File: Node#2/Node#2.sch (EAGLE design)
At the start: 135 parts, among them IC1 TSL25911FN, J1 68712414522, Q1 BC847ALT1SMD, Q2 SI1308EDL-T1-GE3, Q3 FDN304PZ, U2 RV8564C3, U3 BLUENRG-232, U4 TPS63001DRCT, Y3 ECS-160-12-36-AGN-TR, Y4 NX2012SA-32.768K-STD-MUB-1

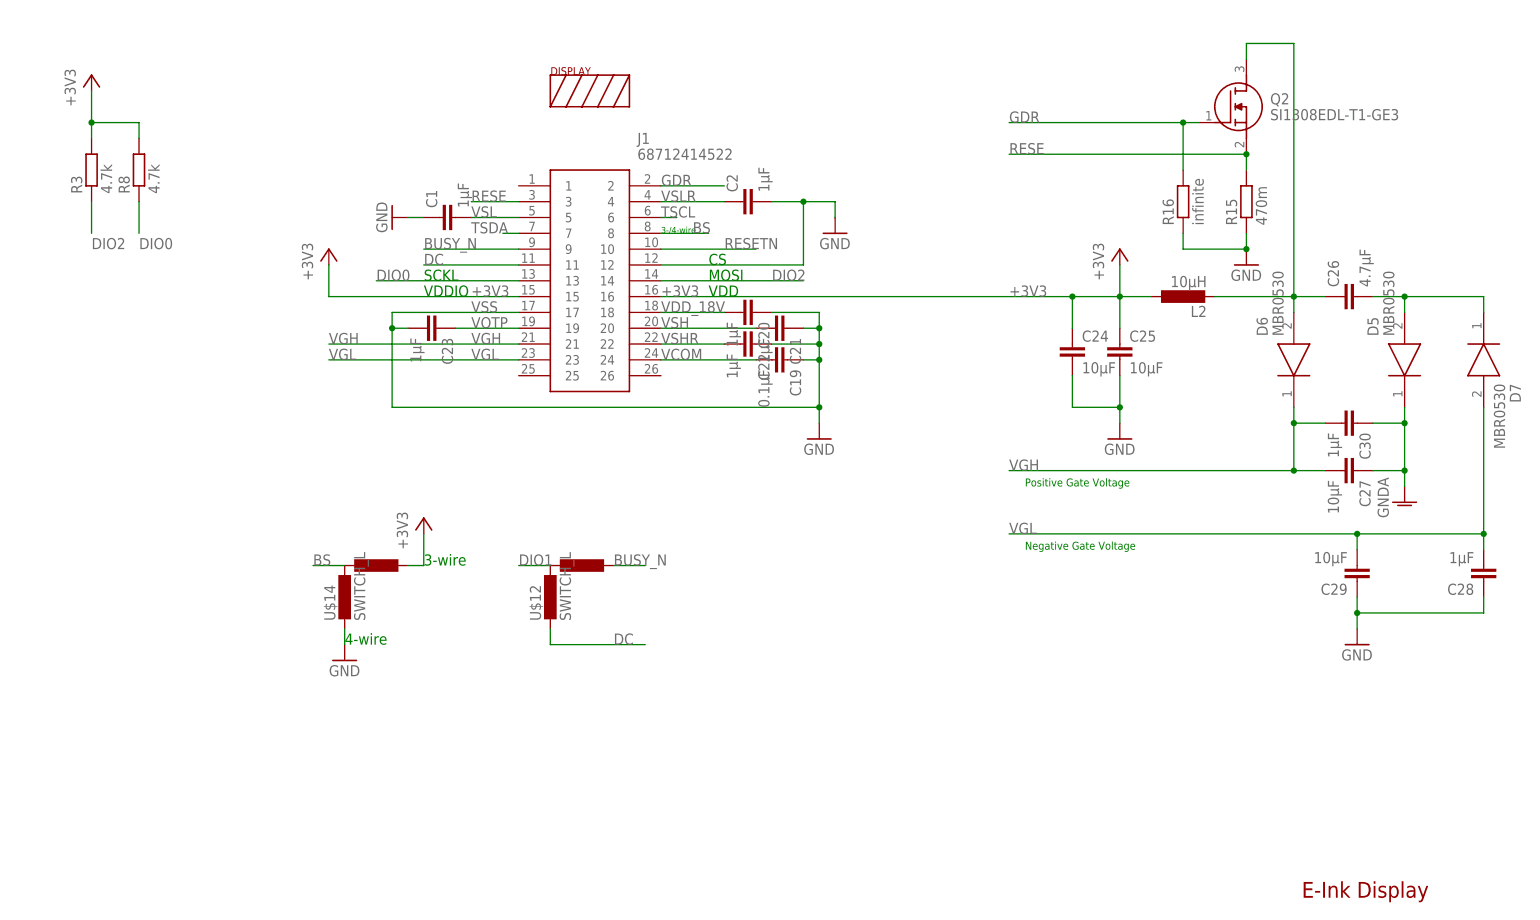
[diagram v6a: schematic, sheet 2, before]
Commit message: Finished Layout Node#2
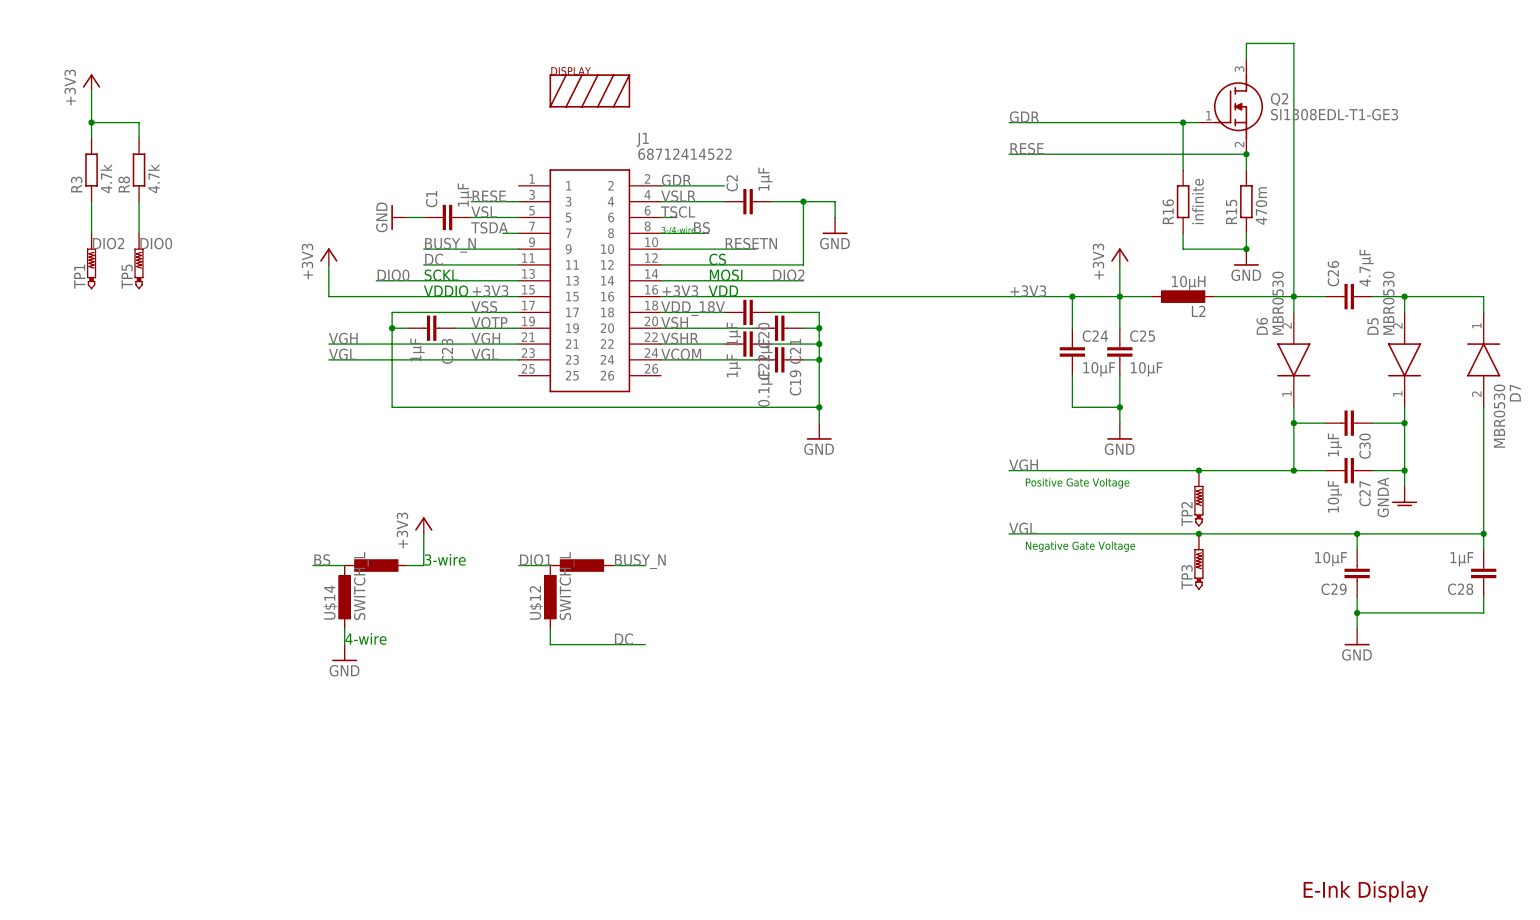
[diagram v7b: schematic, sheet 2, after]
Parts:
- removed D1: ZENER_SMB, BlueHome:ZENER_SMB
- removed U$7: PROXIMITY, BlueHome:PROXIMITY
- removed U$8: WHEEL, BlueHome:WHEEL
- added PROXI: PROXIMITY, BlueHome:PROXIMITY
- added TP1, TP2, TP3, TP4, TP5, TP6: PTR1TP20R, testpad:PTR1TP20R
- added U$18: BZB984_5.4V, BlueHome:BZB984
- added U$19: WHEEL6, BlueHome:WHEEL6
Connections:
- removed net PROX_SENS: U$2.CAP0, U$7.P$1
- removed net SEG4: U$2.CAP6, U$8.SEG4
- new net PROX: PROXI.P$1, U$2.CAP0
- new net PROXI: U$19.SEG$4, U$2.CAP6
- net DIO0: now also TP5.TP
- net DIO2: now also TP1.TP
- net N$14: now also U$18.3; no longer D1.A
- net N$8: now also U$18.2; no longer D1.C
- net SCL: now also TP6.TP
- net SDA: now also TP4.TP
- net SEG1: now also U$19.SEG$1; no longer U$8.SEG1
- net SEG2: now also U$19.SEG$2; no longer U$8.SEG2
- net SEG3: now also U$19.SEG$3; no longer U$8.SEG3
- net SEG5: now also U$19.SEG$5
- net SEG6: now also U$19.SEG$6
- net VGH: now also TP2.TP
- net VGL: now also TP3.TP

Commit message: finished again
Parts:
- D2: value (none) -> DIODE1210; device eagle-ltspice:DIODE_E- -> BlueHome:DIODE1210
- L1: SPICEPREFIX (none) -> L
- R2: value 100 -> 1M
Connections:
- net +3V3_RTC: now also D2.C; no longer D2.A
- net N$1: now also D2.A; no longer D2.C
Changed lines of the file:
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@@
 <grid distance="0.1" unitdist="inch" unit="inch" style="lines" multiple="1" display="no" altdistance="0.01" altunitdist="inch" altunit="inch"/>
 <layers>
-<layer number="1" name="Top" color="4" fill="1" visible="no" active="no"/>
-<layer number="2" name="Route2" color="1" fill="3" visible="no" active="no"/>
-<layer number="3" name="Route3" color="4" fill="3" visible="no" active="no"/>
-<layer number="4" name="Route4" color="1" fill="4" visible="no" active="no"/>
-<layer number="5" name="Route5" color="4" fill="4" visible="no" active="no"/>
-<layer number="6" name="Route6" color="1" fill="8" visible="no" active="no"/>
-<layer number="7" name="Route7" color="4" fill="8" visible="no" active="no"/>
-<layer number="8" name="Route8" color="1" fill="2" visible="no" active="no"/>
-<layer number="9" name="Route9" color="4" fill="2" visible="no" active="no"/>
-<layer number="10" name="Route10" color="1" fill="7" visible="no" active="no"/>
-<layer number="11" name="Route11" color="4" fill="7" visible="no" active="no"/>
-<layer number="12" name="Route12" color="1" fill="5" visible="no" active="no"/>
-<layer number="13" name="Route13" color="4" fill="5" visible="no" active="no"/>
-<layer number="14" name="Route14" color="1" fill="6" visible="no" active="no"/>
-<layer number="15" name="Route15" color="4" fill="6" visible="no" active="no"/>
-<layer number="16" name="Bottom" color="1" fill="1" visible="no" active="no"/>
-<layer number="17" name="Pads" color="2" fill="1" visible="no" active="no"/>
-<layer number="18" name="Vias" color="2" fill="1" visible="no" active="no"/>
-<layer number="19" name="Unrouted" color="6" fill="1" visible="no" active="no"/>
-<layer number="20" name="Dimension" color="15" fill="1" visible="no" active="no"/>
-<layer number="21" name="tPlace" color="7" fill="1" visible="no" active="no"/>
-<layer number="22" name="bPlace" color="7" fill="1" visible="no" active="no"/>
-<layer number="23" name="tOrigins" color="15" fill="1" visible="no" active="no"/>
-<layer number="24" name="bOrigins" color="15" fill="1" visible="no" active="no"/>
-<layer number="25" name="tNames" color="7" fill="1" visible="no" active="no"/>
-<layer number="26" name="bNames" color="7" fill="1" visible="no" active="no"/>
-<layer number="27" name="tValues" color="7" fill="1" visible="no" active="no"/>
-<layer number="28" name="bValues" color="7" fill="1" visible="no" active="no"/>
+<layer number="1" name="Top" color="4" fill="1" visible="yes" active="no"/>
+<layer number="2" name="Route2" color="1" fill="3" visible="yes" active="no"/>
+<layer number="3" name="Route3" color="4" fill="3" visible="yes" active="no"/>
+<layer number="4" name="Route4" color="1" fill="4" visible="yes" active="no"/>
+<layer number="5" name="Route5" color="4" fill="4" visible="yes" active="no"/>
+<layer number="6" name="Route6" color="1" fill="8" visible="yes" active="no"/>
+<layer number="7" name="Route7" color="4" fill="8" visible="yes" active="no"/>
+<layer number="8" name="Route8" color="1" fill="2" visible="yes" active="no"/>
+<layer number="9" name="Route9" color="4" fill="2" visible="yes" active="no"/>
+<layer number="10" name="Route10" color="1" fill="7" visible="yes" active="no"/>
+<layer number="11" name="Route11" color="4" fill="7" visible="yes" active="no"/>
+<layer number="12" name="Route12" color="1" fill="5" visible="yes" active="no"/>
+<layer number="13" name="Route13" color="4" fill="5" visible="yes" active="no"/>
+<layer number="14" name="Route14" color="1" fill="6" visible="yes" active="no"/>
+<layer number="15" name="Route15" color="4" fill="6" visible="yes" active="no"/>
+<layer number="16" name="Bottom" color="1" fill="1" visible="yes" active="no"/>
+<layer number="17" name="Pads" color="2" fill="1" visible="yes" active="no"/>
+<layer number="18" name="Vias" color="2" fill="1" visible="yes" active="no"/>
+<layer number="19" name="Unrouted" color="6" fill="1" visible="yes" active="no"/>
+<layer number="20" name="Dimension" color="15" fill="1" visible="yes" active="no"/>
+<layer number="21" name="tPlace" color="7" fill="1" visible="yes" active="no"/>
+<layer number="22" name="bPlace" color="7" fill="1" visible="yes" active="no"/>
+<layer number="23" name="tOrigins" color="15" fill="1" visible="yes" active="no"/>
+<layer number="24" name="bOrigins" color="15" fill="1" visible="yes" active="no"/>
+<layer number="25" name="tNames" color="7" fill="1" visible="yes" active="no"/>
+<layer number="26" name="bNames" color="7" fill="1" visible="yes" active="no"/>
+<layer number="27" name="tValues" color="7" fill="1" visible="yes" active="no"/>
+<layer number="28" name="bValues" color="7" fill="1" visible="yes" active="no"/>
 <layer number="29" name="tStop" color="7" fill="3" visible="no" active="no"/>
 <layer number="30" name="bStop" color="7" fill="6" visible="no" active="no"/>
@@
 <layer number="35" name="tGlue" color="7" fill="4" visible="no" active="no"/>
 <layer number="36" name="bGlue" color="7" fill="5" visible="no" active="no"/>
-<layer number="37" name="tTest" color="7" fill="1" visible="no" active="no"/>
-<layer number="38" name="bTest" color="7" fill="1" visible="no" active="no"/>
+<layer number="37" name="tTest" color="7" fill="1" visible="yes" active="no"/>
+<layer number="38" name="bTest" color="7" fill="1" visible="yes" active="no"/>
 <layer number="39" name="tKeepout" color="4" fill="11" visible="no" active="no"/>
 <layer number="40" name="bKeepout" color="1" fill="11" visible="no" active="no"/>
@@
 <layer number="44" name="Drills" color="7" fill="1" visible="no" active="no"/>
 <layer number="45" name="Holes" color="7" fill="1" visible="no" active="no"/>
-<layer number="46" name="Milling" color="3" fill="1" visible="no" active="no"/>
-<layer number="47" name="Measures" color="7" fill="1" visible="no" active="no"/>
-<layer number="48" name="Document" color="7" fill="1" visible="no" active="no"/>
-<layer number="49" name="Reference" color="7" fill="1" visible="no" active="no"/>
-<layer number="51" name="tDocu" color="7" fill="1" visible="no" active="no"/>
-<layer number="52" name="bDocu" color="7" fill="1" visible="no" active="no"/>
+<layer number="46" name="Milling" color="3" fill="1" visible="yes" active="no"/>
+<layer number="47" name="Measures" color="7" fill="1" visible="yes" active="no"/>
+<layer number="48" name="Document" color="7" fill="1" visible="yes" active="no"/>
+<layer number="49" name="Reference" color="7" fill="1" visible="yes" active="no"/>
+<layer number="51" name="tDocu" color="7" fill="1" visible="yes" active="no"/>
+<layer number="52" name="bDocu" color="7" fill="1" visible="yes" active="no"/>
 <layer number="88" name="SimResults" color="9" fill="1" visible="no" active="yes"/>
 <layer number="89" name="SimProbes" color="9" fill="1" visible="no" active="yes"/>
@@
 <part name="C7" library="rcl" deviceset="C-EU" device="C0805" value="1u"/>
 <part name="C8" library="rcl" deviceset="C-EU" device="C0805" value="100n"/>
-<part name="L1" library="rcl" deviceset="L-EU" device="L5038P" value="2.2u"/>
+<part name="L1" library="rcl" deviceset="L-EU" device="L5038P" value="2.2u">
+<attribute name="SPICEPREFIX" value="L"/>
+</part>
 <part name="C4" library="rcl" deviceset="C-EU" device="C0805" value="10u"/>
 <part name="C9" library="rcl" deviceset="C-EU" device="C0805" value="10u"/>
@@
 </part>
 <part name="Q3" library="BlueHome" deviceset="FDN304PZ" device=""/>
-<part name="D2" library="eagle-ltspice" deviceset="DIODE_E-" device=""/>
+<part name="D2" library="BlueHome" deviceset="DIODE1210" device=""/>
 <part name="C3" library="rcl" deviceset="C-EU" device="050-055X075" value="100mF"/>
 <part name="GND22" library="supply1" library_urn="urn:adsk.eagle:library:371" deviceset="GND" device=""/>
-<part name="R2" library="rcl" deviceset="R-EU_" device="R0805" value="100"/>
+<part name="R2" library="rcl" deviceset="R-EU_" device="R0805" value="1M"/>
 <part name="P+4" library="supply1" library_urn="urn:adsk.eagle:library:371" deviceset="V+" device=""/>
 <part name="U$9" library="BlueHome" deviceset="BZB984" device=""/>
@@
 <attribute name="VALUE" x="152.4" y="114.3" size="1.778" layer="96"/>
 </instance>
-<instance part="D2" gate="G$1" x="68.58" y="58.42" smashed="yes">
-<attribute name="NAME" x="71.12" y="58.9026" size="1.778" layer="95"/>
-<attribute name="VALUE" x="71.12" y="56.1086" size="1.778" layer="96"/>
+<instance part="D2" gate="G$1" x="68.58" y="58.42" smashed="yes" rot="R270">
+<attribute name="NAME" x="69.0626" y="55.88" size="1.778" layer="95" rot="R270"/>
+<attribute name="VALUE" x="66.2686" y="55.88" size="1.778" layer="96" rot="R270"/>
 </instance>
 <instance part="C3" gate="G$1" x="68.58" y="40.64" smashed="yes">
@@
 <pinref part="C3" gate="G$1" pin="1"/>
 <wire x1="68.58" y1="50.8" x2="68.58" y2="43.18" width="0.1524" layer="91"/>
-<junction x="68.58" y="50.8"/>
 <pinref part="U$9" gate="G$1" pin="2"/>
 <wire x1="78.74" y1="40.64" x2="78.74" y2="50.8" width="0.1524" layer="91"/>
 <wire x1="78.74" y1="50.8" x2="68.58" y2="50.8" width="0.1524" layer="91"/>
-<pinref part="D2" gate="G$1" pin="A"/>
-<wire x1="68.58" y1="55.88" x2="68.58" y2="50.8" width="0.1524" layer="91"/>
 <label x="86.36" y="50.8" size="1.778" layer="95"/>
 <wire x1="78.74" y1="50.8" x2="91.44" y2="50.8" width="0.1524" layer="91"/>
 <junction x="78.74" y="50.8"/>
+<pinref part="D2" gate="G$1" pin="C"/>
+<wire x1="68.58" y1="55.88" x2="68.58" y2="50.8" width="0.1524" layer="91"/>
+<junction x="68.58" y="50.8"/>
 </segment>
 </net>
 <net name="N$1" class="0">
 <segment>
-<pinref part="D2" gate="G$1" pin="C"/>
+<pinref part="D2" gate="G$1" pin="A"/>
 <pinref part="R2" gate="G$1" pin="1"/>
 <wire x1="68.58" y1="60.96" x2="68.58" y2="63.5" width="0.1524" layer="91"/>
